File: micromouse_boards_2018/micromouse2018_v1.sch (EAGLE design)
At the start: 57 parts, among them IC1 TPS562210DDFT

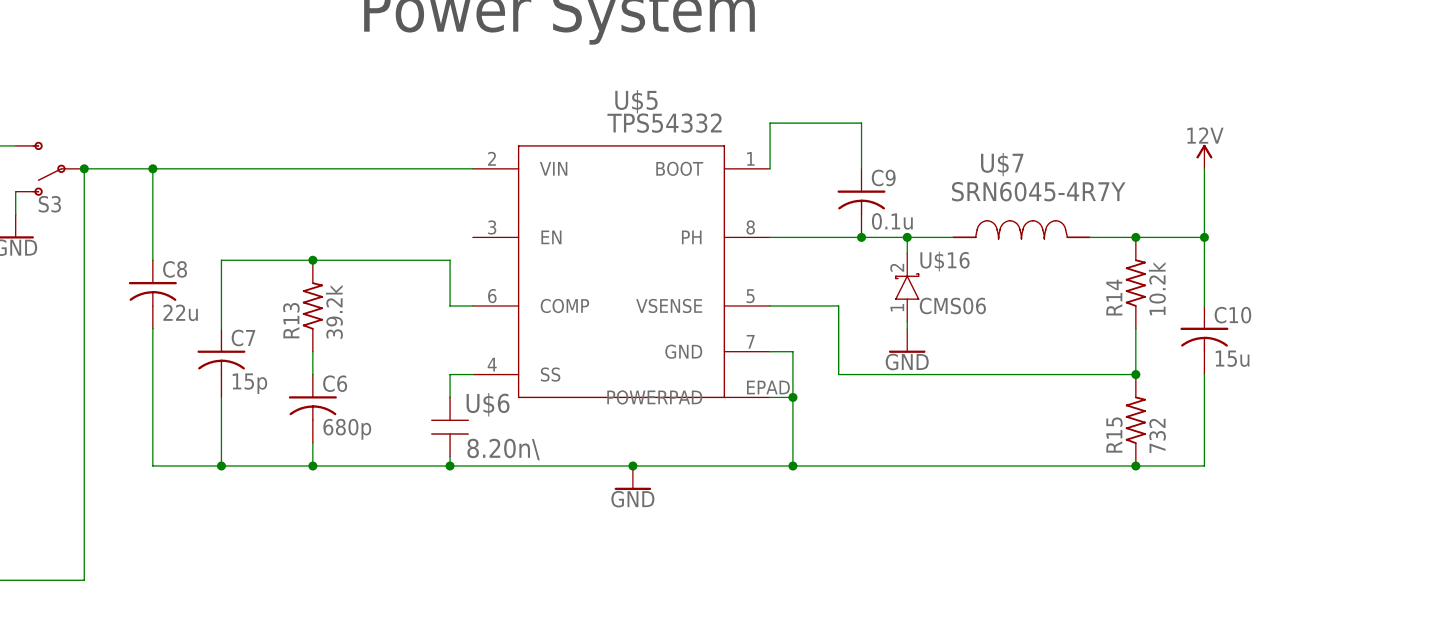
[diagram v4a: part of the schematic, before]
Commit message: Created 12V layout, removed thermals on 5V layout
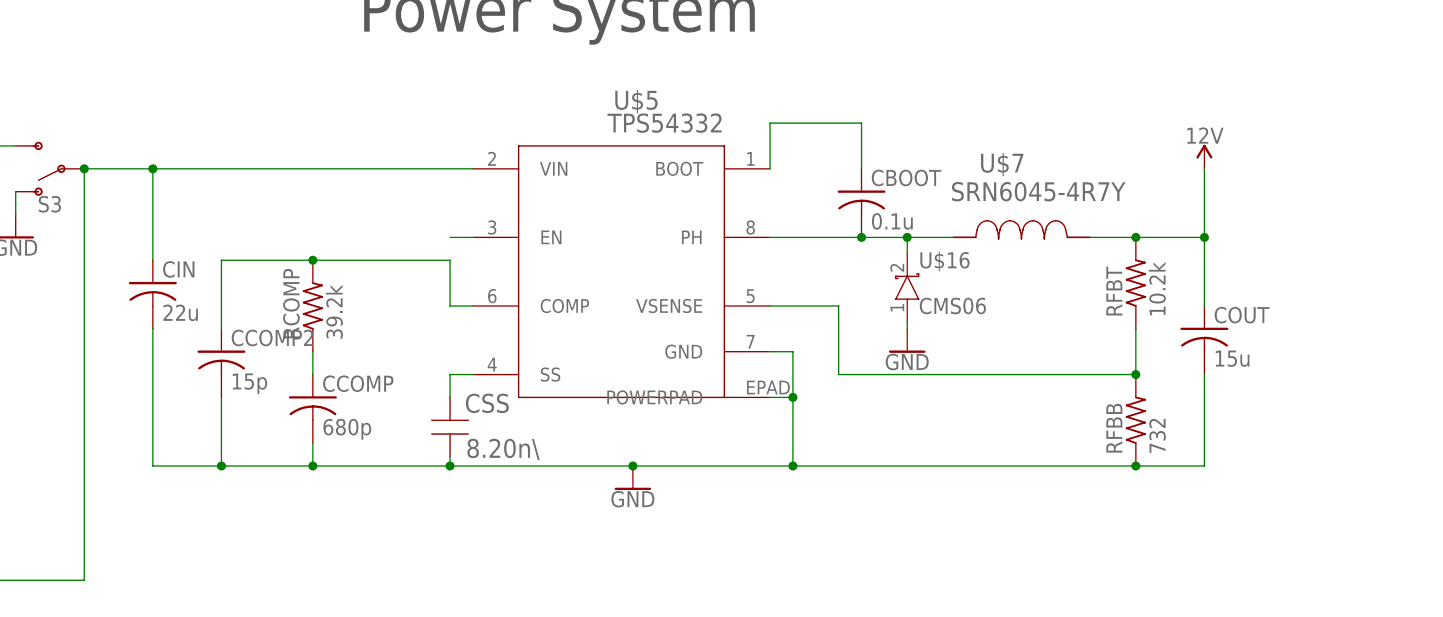
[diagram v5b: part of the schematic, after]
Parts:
- renumbered C10 to COUT, C6 to CCOMP, C7 to CCOMP2, C8 to CIN, C9 to CBOOT, R13 to RCOMP, R14 to RFBT, R15 to RFBB, U$6 to CSS
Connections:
- net N$7 renamed PH
- new net N$8: U$5.EN
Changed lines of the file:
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@@
 <part name="S3" library="SparkFun-Switches" deviceset="SWITCH-SPDT" device="-PTH-11.6X4.0MM"/>
 <part name="U$5" library="TPS54332" deviceset="TPS54332" device=""/>
-<part name="U$6" library="AcceleratedDesigns_Lib" deviceset="12063A822JAT2A" device="" value="8.20n\"/>
-<part name="C6" library="resistor" library_urn="urn:adsk.eagle:library:348" deviceset="C-US" device="C0805" package3d_urn="urn:adsk.eagle:package:26137/1" value="680p"/>
-<part name="C7" library="resistor" library_urn="urn:adsk.eagle:library:348" deviceset="C-US" device="C0805" package3d_urn="urn:adsk.eagle:package:26137/1" value="15p"/>
-<part name="R13" library="resistor" library_urn="urn:adsk.eagle:library:348" deviceset="R-US_" device="R0805" package3d_urn="urn:adsk.eagle:package:26059/1" value="39.2k"/>
-<part name="C8" library="rcl" library_urn="urn:adsk.eagle:library:334" deviceset="C-US" device="C1210" package3d_urn="urn:adsk.eagle:package:23619/2" value="22u"/>
-<part name="C9" library="resistor" library_urn="urn:adsk.eagle:library:348" deviceset="C-US" device="C0805" package3d_urn="urn:adsk.eagle:package:26137/1" value="0.1u"/>
-<part name="C10" library="resistor" library_urn="urn:adsk.eagle:library:348" deviceset="C-US" device="C0805" package3d_urn="urn:adsk.eagle:package:26137/1" value="15u"/>
-<part name="R14" library="resistor" library_urn="urn:adsk.eagle:library:348" deviceset="R-US_" device="R0805" package3d_urn="urn:adsk.eagle:package:26059/1" value="10.2k"/>
-<part name="R15" library="resistor" library_urn="urn:adsk.eagle:library:348" deviceset="R-US_" device="R0805" package3d_urn="urn:adsk.eagle:package:26059/1" value="732"/>
+<part name="CSS" library="AcceleratedDesigns_Lib" deviceset="12063A822JAT2A" device="" value="8.20n\"/>
+<part name="CCOMP" library="resistor" library_urn="urn:adsk.eagle:library:348" deviceset="C-US" device="C0805" package3d_urn="urn:adsk.eagle:package:26137/1" value="680p"/>
+<part name="CCOMP2" library="resistor" library_urn="urn:adsk.eagle:library:348" deviceset="C-US" device="C0805" package3d_urn="urn:adsk.eagle:package:26137/1" value="15p"/>
+<part name="RCOMP" library="resistor" library_urn="urn:adsk.eagle:library:348" deviceset="R-US_" device="R0805" package3d_urn="urn:adsk.eagle:package:26059/1" value="39.2k"/>
+<part name="CIN" library="rcl" library_urn="urn:adsk.eagle:library:334" deviceset="C-US" device="C1210" package3d_urn="urn:adsk.eagle:package:23619/2" value="22u"/>
+<part name="CBOOT" library="resistor" library_urn="urn:adsk.eagle:library:348" deviceset="C-US" device="C0805" package3d_urn="urn:adsk.eagle:package:26137/1" value="0.1u"/>
+<part name="COUT" library="resistor" library_urn="urn:adsk.eagle:library:348" deviceset="C-US" device="C0805" package3d_urn="urn:adsk.eagle:package:26137/1" value="15u"/>
+<part name="RFBT" library="resistor" library_urn="urn:adsk.eagle:library:348" deviceset="R-US_" device="R0805" package3d_urn="urn:adsk.eagle:package:26059/1" value="10.2k"/>
+<part name="RFBB" library="resistor" library_urn="urn:adsk.eagle:library:348" deviceset="R-US_" device="R0805" package3d_urn="urn:adsk.eagle:package:26059/1" value="732"/>
 <part name="U$7" library="AcceleratedDesigns_Lib" deviceset="SRN6045-4R7Y" device=""/>
 <part name="GND15" library="SparkFun-PowerSymbols" deviceset="GND" device=""/>
@@
 <instance part="S3" gate="1" x="256.54" y="111.76" rot="R180"/>
 <instance part="U$5" gate="G$1" x="289.56" y="109.22"/>
-<instance part="U$6" gate="A" x="299.72" y="81.28" smashed="yes" rot="R270">
+<instance part="CSS" gate="A" x="299.72" y="81.28" smashed="yes" rot="R270">
 <attribute name="NAME" x="301.3356" y="84.6586" size="2.0828" layer="95" ratio="6" rot="SR0"/>
 <attribute name="VALUE" x="301.4706" y="79.6486" size="2.0828" layer="96" ratio="6" rot="SR0"/>
 </instance>
-<instance part="C6" gate="G$1" x="284.48" y="86.36"/>
-<instance part="C7" gate="G$1" x="274.32" y="91.44"/>
-<instance part="R13" gate="G$1" x="284.48" y="96.52" rot="R90"/>
-<instance part="C8" gate="G$1" x="266.7" y="99.06"/>
-<instance part="C9" gate="G$1" x="345.44" y="109.22"/>
-<instance part="C10" gate="G$1" x="383.54" y="93.98"/>
-<instance part="R14" gate="G$1" x="375.92" y="99.06" rot="R90"/>
-<instance part="R15" gate="G$1" x="375.92" y="83.82" rot="R90"/>
+<instance part="CCOMP" gate="G$1" x="284.48" y="86.36"/>
+<instance part="CCOMP2" gate="G$1" x="274.32" y="91.44"/>
+<instance part="RCOMP" gate="G$1" x="284.48" y="96.52" rot="R90"/>
+<instance part="CIN" gate="G$1" x="266.7" y="99.06"/>
+<instance part="CBOOT" gate="G$1" x="345.44" y="109.22"/>
+<instance part="COUT" gate="G$1" x="383.54" y="93.98"/>
+<instance part="RFBT" gate="G$1" x="375.92" y="99.06" rot="R90"/>
+<instance part="RFBB" gate="G$1" x="375.92" y="83.82" rot="R90"/>
 <instance part="U$7" gate="A" x="363.22" y="104.14" smashed="yes">
 <attribute name="NAME" x="358.4956" y="111.3536" size="2.0828" layer="95" ratio="6" rot="SR0"/>
@@
 <segment>
 <pinref part="U$7" gate="A" pin="2"/>
-<pinref part="R14" gate="G$1" pin="2"/>
+<pinref part="RFBT" gate="G$1" pin="2"/>
 <wire x1="370.84" y1="104.14" x2="375.92" y2="104.14" width="0.1524" layer="91"/>
-<pinref part="C10" gate="G$1" pin="1"/>
+<pinref part="COUT" gate="G$1" pin="1"/>
 <wire x1="375.92" y1="104.14" x2="383.54" y2="104.14" width="0.1524" layer="91"/>
 <wire x1="383.54" y1="104.14" x2="383.54" y2="96.52" width="0.1524" layer="91"/>
@@
 </segment>
 <segment>
-<pinref part="R15" gate="G$1" pin="1"/>
+<pinref part="RFBB" gate="G$1" pin="1"/>
 <wire x1="375.92" y1="78.74" x2="337.82" y2="78.74" width="0.1524" layer="91"/>
 <pinref part="U$5" gate="G$1" pin="GND"/>
@@
 <wire x1="337.82" y1="86.36" x2="337.82" y2="78.74" width="0.1524" layer="91"/>
 <wire x1="320.04" y1="78.74" x2="299.72" y2="78.74" width="0.1524" layer="91"/>
-<pinref part="U$6" gate="A" pin="1"/>
+<pinref part="CSS" gate="A" pin="1"/>
 <wire x1="299.72" y1="79.756" x2="299.72" y2="78.74" width="0.1524" layer="91"/>
-<pinref part="C8" gate="G$1" pin="2"/>
+<pinref part="CIN" gate="G$1" pin="2"/>
 <wire x1="299.72" y1="78.74" x2="284.48" y2="78.74" width="0.1524" layer="91"/>
 <wire x1="284.48" y1="78.74" x2="274.32" y2="78.74" width="0.1524" layer="91"/>
@@
 <wire x1="266.7" y1="78.74" x2="266.7" y2="93.98" width="0.1524" layer="91"/>
 <junction x="299.72" y="78.74"/>
-<pinref part="C7" gate="G$1" pin="2"/>
+<pinref part="CCOMP2" gate="G$1" pin="2"/>
 <wire x1="274.32" y1="86.36" x2="274.32" y2="78.74" width="0.1524" layer="91"/>
 <junction x="274.32" y="78.74"/>
-<pinref part="C6" gate="G$1" pin="2"/>
+<pinref part="CCOMP" gate="G$1" pin="2"/>
 <wire x1="284.48" y1="81.28" x2="284.48" y2="78.74" width="0.1524" layer="91"/>
 <junction x="284.48" y="78.74"/>
-<pinref part="C10" gate="G$1" pin="2"/>
+<pinref part="COUT" gate="G$1" pin="2"/>
 <wire x1="383.54" y1="88.9" x2="383.54" y2="78.74" width="0.1524" layer="91"/>
 <wire x1="383.54" y1="78.74" x2="375.92" y2="78.74" width="0.1524" layer="91"/>
@@
 </segment>
 </net>
-<net name="N$7" class="0">
-<segment>
-<pinref part="C9" gate="G$1" pin="2"/>
+<net name="PH" class="0">
+<segment>
+<pinref part="CBOOT" gate="G$1" pin="2"/>
 <pinref part="U$5" gate="G$1" pin="PH"/>
 <wire x1="335.28" y1="104.14" x2="345.44" y2="104.14" width="0.1524" layer="91"/>
@@
 <net name="N$9" class="0">
 <segment>
-<pinref part="R14" gate="G$1" pin="1"/>
-<pinref part="R15" gate="G$1" pin="2"/>
+<pinref part="RFBT" gate="G$1" pin="1"/>
+<pinref part="RFBB" gate="G$1" pin="2"/>
 <wire x1="375.92" y1="93.98" x2="375.92" y2="88.9" width="0.1524" layer="91"/>
 <pinref part="U$5" gate="G$1" pin="VSENSE"/>
@@
 <pinref part="U$5" gate="G$1" pin="BOOT"/>
 <wire x1="335.28" y1="111.76" x2="335.28" y2="116.84" width="0.1524" layer="91"/>
-<pinref part="C9" gate="G$1" pin="1"/>
+<pinref part="CBOOT" gate="G$1" pin="1"/>
 <wire x1="335.28" y1="116.84" x2="345.44" y2="116.84" width="0.1524" layer="91"/>
 <wire x1="345.44" y1="116.84" x2="345.44" y2="111.76" width="0.1524" layer="91"/>
@@
 <segment>
 <pinref part="U$5" gate="G$1" pin="SS"/>
-<pinref part="U$6" gate="A" pin="2"/>
+<pinref part="CSS" gate="A" pin="2"/>
 <wire x1="302.26" y1="88.9" x2="299.72" y2="88.9" width="0.1524" layer="91"/>
 <wire x1="299.72" y1="88.9" x2="299.72" y2="86.36" width="0.1524" layer="91"/>
@@
 <net name="N$11" class="0">
 <segment>
-<pinref part="C7" gate="G$1" pin="1"/>
+<pinref part="CCOMP2" gate="G$1" pin="1"/>
 <wire x1="274.32" y1="93.98" x2="274.32" y2="101.6" width="0.1524" layer="91"/>
-<pinref part="R13" gate="G$1" pin="2"/>
+<pinref part="RCOMP" gate="G$1" pin="2"/>
 <wire x1="274.32" y1="101.6" x2="284.48" y2="101.6" width="0.1524" layer="91"/>
 <wire x1="284.48" y1="101.6" x2="299.72" y2="101.6" width="0.1524" layer="91"/>
@@
 <net name="N$12" class="0">
 <segment>
-<pinref part="R13" gate="G$1" pin="1"/>
-<pinref part="C6" gate="G$1" pin="1"/>
+<pinref part="RCOMP" gate="G$1" pin="1"/>
+<pinref part="CCOMP" gate="G$1" pin="1"/>
 <wire x1="284.48" y1="91.44" x2="284.48" y2="88.9" width="0.1524" layer="91"/>
 </segment>
@@
 <wire x1="208.28" y1="66.04" x2="208.28" y2="48.26" width="0.1524" layer="91"/>
 <junction x="208.28" y="48.26"/>
-<pinref part="C8" gate="G$1" pin="1"/>
+<pinref part="CIN" gate="G$1" pin="1"/>
 <wire x1="266.7" y1="101.6" x2="266.7" y2="111.76" width="0.1524" layer="91"/>
 <pinref part="U$5" gate="G$1" pin="VIN"/>
@@
 </segment>
 </net>
+<net name="N$8" class="0">
+<segment>
+<pinref part="U$5" gate="G$1" pin="EN"/>
+<wire x1="302.26" y1="104.14" x2="299.72" y2="104.14" width="0.1524" layer="91"/>
+</segment>
+</net>

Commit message: Completed Board layout, passed DRC, removed 2 status LEDs, increased C6 C7
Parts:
- removed C4, C5: 1.0uF, SparkFun-Capacitors:1.0UF-0805-25V-10%
- removed D1, D4: (no value), SparkFun-LED:LED0603
- removed R2: 1k, SparkFun-Resistors:1KOHM-0603-1/10W-1%
- removed R5: 330, SparkFun-Resistors:330OHM-0603-1/10W-1%
- removed S3: (no value), SparkFun-Switches:SWITCH-SPDT-PTH-11.6X4.0MM
- added C6, C7: 100uF, SparkFun-Capacitors:100UF-POLAR-25V-20%(ELEC)
- added GND, H1: MOUNT-PAD-SQUARE3.6, holes:MOUNT-PAD-SQUARE3.6
- added U$6: ULTRASONIC, raParts:ULTRASONIC
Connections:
- removed net DIRECTION: U$2.DIRECTION
- removed net N$1: D1.A, R2.2
- removed net N$4: D4.A, R5.2
- removed net V_BATT: D1.C, S3.S
- new net ECHO3: B1.10*/TX2/CS, U$6.ECHO
- new net TRIG3: B1.11/DOUT, U$6.TRIG
- net 12V: now also C6.+, C7.+, D2.A; no longer C4.1, C5.1, D2.C
- net 3.3V: no longer D4.C
- net 5V: now also D3.A, U$6.VCC; no longer D3.C
- net DIRECTION1: now also B1.6*, U$2.DIRECTION; no longer B1.7/RX3
- net DIRECTION2: now also B1.7/RX3; no longer B1.8/TX3
- net ECHO1: now also B1.8/TX3
- net ECHO2: now also B1.2
- net GND: now also C6.-, C7.-, U$6.GND; no longer C4.2, C5.2, R2.1, R5.1, S3.O
- net N$2: now also D2.C; no longer D2.A
- net N$3: now also D3.C; no longer D3.A
- net STEP1: now also B1.4*; no longer B1.3*
- net STEP2: now also B1.5*; no longer B1.4*
- net TRIG1: now also B1.9*/RX2
- net TRIG2: now also B1.3*
- net VIN: now also H1.MOUNT; no longer S3.P
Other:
- note added: "// Check wire gauge to decide mounting hole size"
- moved on the sheet: CBOOT, CCOMP, CCOMP2, CIN, COUT, CSS, D2, D3, RCOMP, RFBB, RFBT, U$16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

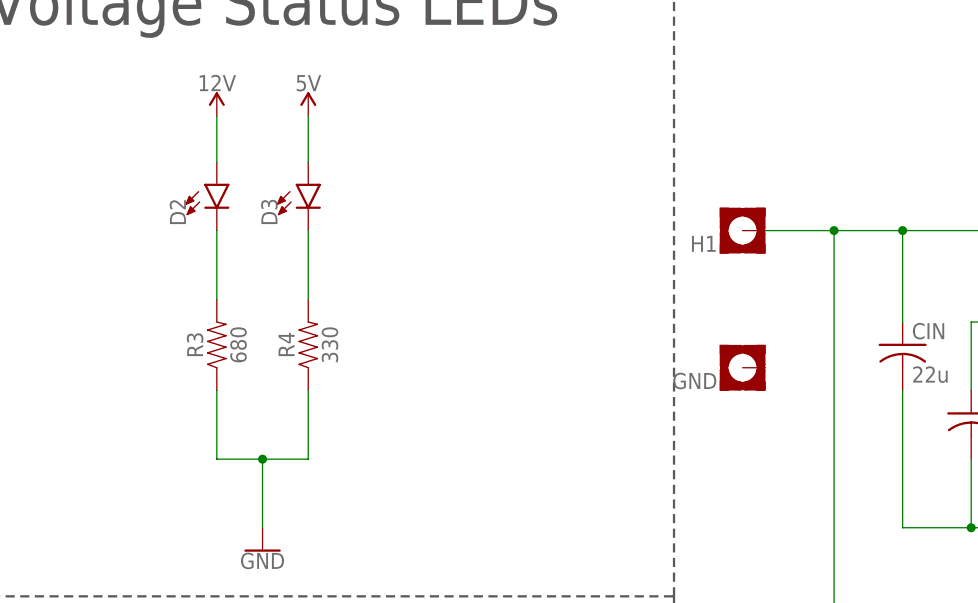
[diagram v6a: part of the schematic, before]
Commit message: Fixed some silkscreen labels
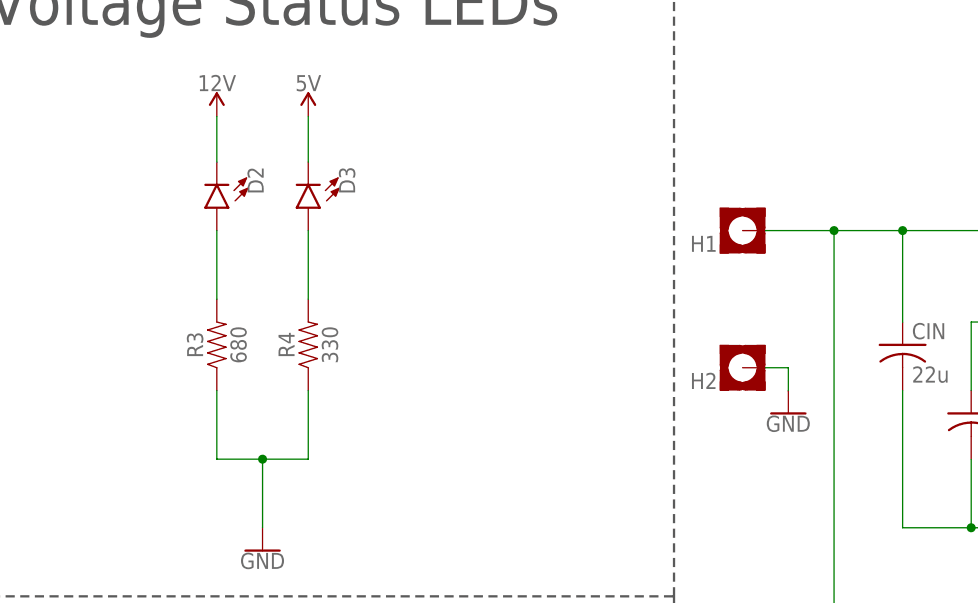
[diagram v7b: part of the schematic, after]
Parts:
- renumbered GND to H2
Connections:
- removed net N$3: D3.C, R4.2
- new net N$1: D2.A, R3.2
- net 12V: now also D2.C; no longer D2.A
- net 5V: now also D3.C; no longer D3.A
- net GND: now also H2.MOUNT
- net N$2: now also D3.A, R4.2; no longer D2.C, R3.2
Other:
- moved on the sheet: D2, D3
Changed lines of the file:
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@@
 <part name="U$16" library="Scraps" deviceset="CMS06" device=""/>
 <part name="H1" library="holes" library_urn="urn:adsk.eagle:library:237" deviceset="MOUNT-PAD-SQUARE" device="3.6" package3d_urn="urn:adsk.eagle:package:14294/1"/>
-<part name="GND" library="holes" library_urn="urn:adsk.eagle:library:237" deviceset="MOUNT-PAD-SQUARE" device="3.6" package3d_urn="urn:adsk.eagle:package:14294/1"/>
+<part name="H2" library="holes" library_urn="urn:adsk.eagle:library:237" deviceset="MOUNT-PAD-SQUARE" device="3.6" package3d_urn="urn:adsk.eagle:package:14294/1"/>
 <part name="U$6" library="raParts" deviceset="ULTRASONIC" device=""/>
 <part name="SUPPLY23" library="SparkFun-PowerSymbols" deviceset="5V" device=""/>
@@
 <part name="C6" library="SparkFun-Capacitors" deviceset="100UF-POLAR" device="-25V-20%(ELEC)" value="100uF"/>
 <part name="C7" library="SparkFun-Capacitors" deviceset="100UF-POLAR" device="-25V-20%(ELEC)" value="100uF"/>
+<part name="GND18" library="SparkFun-PowerSymbols" deviceset="GND" device=""/>
 </parts>
 <sheets>
@@
 <instance part="SUPPLY2" gate="G$1" x="12.7" y="50.8"/>
 <instance part="GND1" gate="1" x="33.02" y="12.7"/>
-<instance part="D2" gate="G$1" x="139.7" y="109.22"/>
-<instance part="D3" gate="G$1" x="149.86" y="109.22"/>
+<instance part="D2" gate="G$1" x="139.7" y="106.68" rot="R180"/>
+<instance part="D3" gate="G$1" x="149.86" y="106.68" rot="R180"/>
 <instance part="GND2" gate="1" x="144.78" y="68.58"/>
 <instance part="SUPPLY3" gate="G$1" x="149.86" y="116.84"/>
@@
 <attribute name="NAME" x="195.326" y="103.5558" size="1.778" layer="95" rot="R180"/>
 </instance>
-<instance part="GND" gate="G$1" x="198.12" y="88.9" smashed="yes" rot="R180">
+<instance part="H2" gate="G$1" x="198.12" y="88.9" smashed="yes" rot="R180">
 <attribute name="NAME" x="195.326" y="88.3158" size="1.778" layer="95" rot="R180"/>
 </instance>
@@
 <instance part="C6" gate="G$1" x="162.56" y="27.94"/>
 <instance part="C7" gate="G$1" x="175.26" y="27.94"/>
+<instance part="GND18" gate="1" x="203.2" y="83.82"/>
 </instances>
 <busses>
@@
 <segment>
 <pinref part="SUPPLY5" gate="G$1" pin="12V"/>
-<pinref part="D2" gate="G$1" pin="A"/>
+<pinref part="D2" gate="G$1" pin="C"/>
 <wire x1="139.7" y1="116.84" x2="139.7" y2="111.76" width="0.1524" layer="91"/>
 </segment>
@@
 <segment>
 <pinref part="SUPPLY3" gate="G$1" pin="5V"/>
-<pinref part="D3" gate="G$1" pin="A"/>
+<pinref part="D3" gate="G$1" pin="C"/>
 <wire x1="149.86" y1="116.84" x2="149.86" y2="111.76" width="0.1524" layer="91"/>
 </segment>
@@
 <wire x1="378.46" y1="124.46" x2="378.46" y2="134.62" width="0.1524" layer="91"/>
 </segment>
+<segment>
+<pinref part="H2" gate="G$1" pin="MOUNT"/>
+<wire x1="200.66" y1="88.9" x2="203.2" y2="88.9" width="0.1524" layer="91"/>
+<pinref part="GND18" gate="1" pin="GND"/>
+<wire x1="203.2" y1="88.9" x2="203.2" y2="86.36" width="0.1524" layer="91"/>
+</segment>
 </net>
 <net name="ENABLE1" class="0">
@@
 </segment>
 </net>
-<net name="N$2" class="0">
-<segment>
-<pinref part="D2" gate="G$1" pin="C"/>
+<net name="N$1" class="0">
+<segment>
+<pinref part="D2" gate="G$1" pin="A"/>
 <pinref part="R3" gate="G$1" pin="2"/>
 <wire x1="139.7" y1="104.14" x2="139.7" y2="96.52" width="0.1524" layer="91"/>
 </segment>
 </net>
-<net name="N$3" class="0">
-<segment>
-<pinref part="D3" gate="G$1" pin="C"/>
+<net name="N$2" class="0">
+<segment>
+<pinref part="D3" gate="G$1" pin="A"/>
 <pinref part="R4" gate="G$1" pin="2"/>
 <wire x1="149.86" y1="104.14" x2="149.86" y2="96.52" width="0.1524" layer="91"/>
